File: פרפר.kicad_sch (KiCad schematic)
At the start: 33 parts, among them J1 Conn_01x03_MountingPin, J2 Conn_01x22_Shielded

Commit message: parpar v2 RC2
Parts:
- added D49: TI TSD05C, PCM_Diode_SMD_AKL:D_SOD-323_TVS, symbol PCM_Diode_TVS_AKL:D_TVS_Bidirectional_Generic
- added J5: Conn_01x04_MountingPin, Connector_JST:JST_SH_SM04B-SRSS-TB_1x04-1MP_P1.00mm_Horizontal, symbol Connector_Generic_MountingPin:Conn_01x04_MountingPin
- added JP2: SolderJumper_3_Bridged12, Jumper:SolderJumper-3_P1.3mm_Bridged12_RoundedPad1.0x1.5mm, symbol Jumper:SolderJumper_3_Bridged12
- J1: footprint Connector_JST:JST_PH_S3B-PH-SM4-TB_1x03-1MP_P2.00mm_Horizontal -> Connector_JST:JST_SH_BM03B-SRSS-TB_1x03-1MP_P1.00mm_Vertical
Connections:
- net GND: now also D49.2 (A), J5.1 (Pin_1), J5.MP (MountPin)
- net PRI_LO: now also J5.2 (Pin_2)
- net ec1a: no longer D47.6 (L4)
- net ec1b: no longer D47.4 (L3)
- net ec2a: no longer D47.3 (L2)
- net ec2b: no longer D47.1 (L1)
- net gpio3: now also JP2.1 (A)
- net gpio4: now also J5.4 (Pin_4)
- net c0 renamed col_a
- net c1 renamed col_b
- net c2 renamed col_c
- net c3 renamed col_d
- net c4 renamed col_e
- net c5 renamed col_f
- net row_a renamed row_0
- net row_b renamed row_1
- net row_c renamed row_2
- net row_d renamed row_3
- net row_e renamed row_4
- net row_f renamed row_5
- net row_g renamed row_6
- net row_h renamed row_7
- new net: J5.3 (Pin_3), JP2.2 (C)
- new net emtx_b0: D47.6 (L4)
- new net emtx_b1: D47.4 (L3)
- new net emtx_c0: D47.3 (L2)
- new net emtx_c1: D47.1 (L1)
- new net led_data: D49.1 (K)
- new net led_out: JP2.3 (B)
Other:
- note added: "add-on port"
- note added: "led input"
- note removed: "led power input"
- moved on the sheet: D48

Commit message: parpar v2 RC3
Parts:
- removed JP2: SolderJumper_3_Bridged12, Jumper:SolderJumper-3_P1.3mm_Bridged12_RoundedPad1.0x1.5mm, symbol Jumper:SolderJumper_3_Bridged12
- added J6: Conn_01x02_MountingPin, Connector_JST:JST_SUR_SM02B-SURS-TF_1x02-1MP_P0.80mm_Horizontal, symbol Connector_Generic_MountingPin:Conn_01x02_MountingPin
- added JP2, JP4, JP5: SolderJumper_3_Open, Jumper:SolderJumper-3_P2.0mm_Open_TrianglePad1.0x1.5mm, symbol Jumper:SolderJumper_3_Open
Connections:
- net emtx_b0 is gone; now on net ec1a: D47.6 (L4)
- net emtx_b1 is gone; now on net ec1b: D47.4 (L3)
- net emtx_c0 is gone; now on net ec2a: D47.3 (L2)
- net emtx_c1 is gone; now on net ec2b: D47.1 (L1)
- net GND: now also J6.MP (MountPin), JP5.3 (B); no longer J5.1 (Pin_1)
- net PRI_LO: now also JP4.3 (B); no longer J5.2 (Pin_2)
- net gpio3: now also JP2.1 (A)
- net led_out: now also JP2.3 (B)
- net at J5.3 (Pin_3): now also JP2.2 (C)
- new net: J5.2 (Pin_2), JP4.2 (C)
- new net: J5.1 (Pin_1), JP5.2 (C)
- new net Earth_Clean: J6.2 (Pin_2), JP5.1 (A)
- new net VCC: J6.1 (Pin_1), JP4.1 (A)
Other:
- note added: "mcu vdd in"
- moved on the sheet: J5

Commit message: parpar v2 RC4
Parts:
- removed H1: MountingHole, MountingHole:MountingHole_2.2mm_M2_DIN965, symbol Mechanical:MountingHole
- removed JP5: SolderJumper_3_Open, Jumper:SolderJumper-3_P2.0mm_Open_TrianglePad1.0x1.5mm, symbol Jumper:SolderJumper_3_Open
- added FB3: Ferrite_Bead, PCM_Ferrite_SMD_AKL:Ferrite_0805_2012Metric, symbol PCM_Device_AKL:Ferrite_Bead
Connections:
- net PRI_LO is gone; now on net +5V: D48.1 (K), JP4.3 (B)
- net Earth_Clean: now also FB3.1
- net GND: now also J5.1 (Pin_1), FB3.2
- net led_data renamed led_data_in
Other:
- note removed: "alignment mounting hole"
- moved on the sheet: D1, D2, D45, D46, D47, D48, D49, FB1, FB2, H10, H11, H12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

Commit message: parpar v2 RC6
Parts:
- added J7: JST_SH_BM03B-SRSS-TB, Connector_JST:JST_SH_BM03B-SRSS-TB_1x03-1MP_P1.00mm_Vertical, symbol Connector_Generic_MountingPin:Conn_01x03_MountingPin
- J1: value Conn_01x03_MountingPin -> JST_SH_BM03B-SRSS-TB
- J2: value Conn_01x22_Shielded -> Hirose_FH12-22S-0.5SH
- J5: value Conn_01x04_MountingPin -> JST_SH_SM04B-SRSS-TB
- J6: value Conn_01x02_MountingPin -> JST_SUR_SM02B-SURS-TF
- JP2: value SolderJumper_3_Open -> data select; footprint Jumper:SolderJumper-3_P2.0mm_Open_TrianglePad1.0x1.5mm -> Jumper:SolderJumper-3_P1.3mm_Bridged12_RoundedPad1.0x1.5mm; symbol Jumper:SolderJumper_3_Open -> Jumper:SolderJumper_3_Bridged12
- JP4: value SolderJumper_3_Open -> power select; footprint Jumper:SolderJumper-3_P2.0mm_Open_TrianglePad1.0x1.5mm -> Jumper:SolderJumper-3_P1.3mm_Bridged12_RoundedPad1.0x1.5mm; symbol Jumper:SolderJumper_3_Open -> Jumper:SolderJumper_3_Bridged12
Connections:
- net +5V: now also J7.2 (Pin_2)
- net GND: now also J7.3 (Pin_3), J7.MP (MountPin)
- net led_out: now also J7.1 (Pin_1)
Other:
- note added: "rgb in"
- note added: "rgb out"
- note removed: "led input"

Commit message: coquette parpar mk2 final?
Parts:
- added RN1, RN2: R_4x0603_Concave, PCM_Resistor_SMD_AKL:R_Array_Concave_4x0603, symbol PCM_Resistor_AKL:R_4x0603_Concave
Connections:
- net row_0: now also RN1.5 (R4.2); no longer D1.6 (L4), J2.2 (Pin_2)
- net row_1: now also RN1.6 (R3.2); no longer D1.3 (L2), J2.3 (Pin_3)
- net row_2: now also RN1.7 (R2.2); no longer D1.1 (L1), J2.4 (Pin_4)
- net row_3: now also RN1.8 (R1.2); no longer D1.4 (L3), J2.5 (Pin_5)
- net row_4: now also RN2.5 (R4.2); no longer D2.6 (L4), J2.18 (Pin_18)
- net row_5: now also RN2.6 (R3.2); no longer D2.4 (L3), J2.19 (Pin_19)
- net row_6: now also RN2.7 (R2.2); no longer D2.3 (L2), J2.20 (Pin_20)
- net row_7: now also RN2.8 (R1.2); no longer D2.1 (L1), J2.21 (Pin_21)
- new net row_0_in: D1.6 (L4), J2.2 (Pin_2), RN1.4 (R4.1)
- new net row_1_in: D1.3 (L2), J2.3 (Pin_3), RN1.3 (R3.1)
- new net row_2_in: D1.1 (L1), J2.4 (Pin_4), RN1.2 (R2.1)
- new net row_3_in: D1.4 (L3), J2.5 (Pin_5), RN1.1 (R1.1)
- new net row_4_in: D2.6 (L4), J2.18 (Pin_18), RN2.4 (R4.1)
- new net row_5_in: D2.4 (L3), J2.19 (Pin_19), RN2.3 (R3.1)
- new net row_6_in: D2.3 (L2), J2.20 (Pin_20), RN2.2 (R2.1)
- new net row_7_in: D2.1 (L1), J2.21 (Pin_21), RN2.1 (R1.1)

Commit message: coquette parpar mk2 final? try2
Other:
- note added: "row series resistors"
- moved on the sheet: RN1, RN2
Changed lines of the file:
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@@
 	)
 	(rectangle
+		(start 215.9 98.425)
+		(end 251.46 160.02)
+		(stroke
+			(width 0)
+			(type default)
+		)
+		(fill
+			(type none)
+		)
+	)
+	(rectangle
 		(start 26.67 97.79)
 		(end 71.12 128.27)
@@
 		)
 	)
+	(text "row series resistors"
+		(exclude_from_sim no)
+		(at 225.298 97.79 0)
+		(effects
+			(font
+				(size 1.27 1.27)
+			)
+		)
+	)
 	(text "rgb in"
 		(exclude_from_sim no)
@@
 	(global_label "row_4"
 		(shape input)
-		(at 237.49 140.97 90)
+		(at 228.6 137.16 90)
 		(fields_autoplaced yes)
 		(effects
@@
 		)
 		(property "Intersheetrefs" "${INTERSHEET_REFS}"
-			(at 237.49 133.6103 90)
+			(at 228.6 129.8003 90)
 			(effects
 				(font
@@
 	(global_label "row_5"
 		(shape input)
-		(at 234.95 140.97 90)
+		(at 226.06 137.16 90)
 		(fields_autoplaced yes)
 		(effects
@@
 		)
 		(property "Intersheetrefs" "${INTERSHEET_REFS}"
-			(at 234.95 133.6103 90)
+			(at 226.06 129.8003 90)
 			(effects
 				(font
@@
 	(global_label "row_6"
 		(shape input)
-		(at 232.41 140.97 90)
+		(at 223.52 137.16 90)
 		(fields_autoplaced yes)
 		(effects
@@
 		)
 		(property "Intersheetrefs" "${INTERSHEET_REFS}"
-			(at 232.41 133.6103 90)
+			(at 223.52 129.8003 90)
 			(effects
 				(font
@@
 	(global_label "row_5_in"
 		(shape input)
-		(at 234.95 151.13 270)
+		(at 226.06 147.32 270)
 		(fields_autoplaced yes)
 		(effects
@@
 		)
 		(property "Intersheetrefs" "${INTERSHEET_REFS}"
-			(at 234.95 161.2479 90)
+			(at 226.06 157.4379 90)
 			(effects
 				(font
@@
 	(global_label "row_1_in"
 		(shape input)
-		(at 234.95 121.92 270)
+		(at 226.06 118.11 270)
 		(fields_autoplaced yes)
 		(effects
@@
 		)
 		(property "Intersheetrefs" "${INTERSHEET_REFS}"
-			(at 234.95 132.0379 90)
+			(at 226.06 128.2279 90)
 			(effects
 				(font
@@
 	(global_label "row_0"
 		(shape input)
-		(at 237.49 111.76 90)
+		(at 228.6 107.95 90)
 		(fields_autoplaced yes)
 		(effects
@@
 		)
 		(property "Intersheetrefs" "${INTERSHEET_REFS}"
-			(at 237.49 104.4003 90)
+			(at 228.6 100.5903 90)
 			(effects
 				(font
@@
 	(global_label "row_3_in"
 		(shape input)
-		(at 229.87 121.92 270)
+		(at 220.98 118.11 270)
 		(fields_autoplaced yes)
 		(effects
@@
 		)
 		(property "Intersheetrefs" "${INTERSHEET_REFS}"
-			(at 229.87 132.0379 90)
+			(at 220.98 128.2279 90)
 			(effects
 				(font
@@
 	(global_label "row_1"
 		(shape input)
-		(at 234.95 111.76 90)
+		(at 226.06 107.95 90)
 		(fields_autoplaced yes)
 		(effects
@@
 		)
 		(property "Intersheetrefs" "${INTERSHEET_REFS}"
-			(at 234.95 104.4003 90)
+			(at 226.06 100.5903 90)
 			(effects
 				(font
@@
 	(global_label "row_2_in"
 		(shape input)
-		(at 232.41 121.92 270)
+		(at 223.52 118.11 270)
 		(fields_autoplaced yes)
 		(effects
@@
 		)
 		(property "Intersheetrefs" "${INTERSHEET_REFS}"
-			(at 232.41 132.0379 90)
+			(at 223.52 128.2279 90)
 			(effects
 				(font
@@
 	(global_label "row_0_in"
 		(shape input)
-		(at 237.49 121.92 270)
+		(at 228.6 118.11 270)
 		(fields_autoplaced yes)
 		(effects
@@
 		)
 		(property "Intersheetrefs" "${INTERSHEET_REFS}"
-			(at 237.49 132.0379 90)
+			(at 228.6 128.2279 90)
 			(effects
 				(font
@@
 	(global_label "row_4_in"
 		(shape input)
-		(at 237.49 151.13 270)
+		(at 228.6 147.32 270)
 		(fields_autoplaced yes)
 		(effects
@@
 		)
 		(property "Intersheetrefs" "${INTERSHEET_REFS}"
-			(at 237.49 161.2479 90)
+			(at 228.6 157.4379 90)
 			(effects
 				(font
@@
 	(global_label "row_3"
 		(shape input)
-		(at 229.87 111.76 90)
+		(at 220.98 107.95 90)
 		(fields_autoplaced yes)
 		(effects
@@
 		)
 		(property "Intersheetrefs" "${INTERSHEET_REFS}"
-			(at 229.87 104.4003 90)
+			(at 220.98 100.5903 90)
 			(effects
 				(font
@@
 	(global_label "row_7_in"
 		(shape input)
-		(at 229.87 151.13 270)
+		(at 220.98 147.32 270)
 		(fields_autoplaced yes)
 		(effects
@@
 		)
 		(property "Intersheetrefs" "${INTERSHEET_REFS}"
-			(at 229.87 161.2479 90)
+			(at 220.98 157.4379 90)
 			(effects
 				(font
@@
 	(global_label "row_2"
 		(shape input)
-		(at 232.41 111.76 90)
+		(at 223.52 107.95 90)
 		(fields_autoplaced yes)
 		(effects
@@
 		)
 		(property "Intersheetrefs" "${INTERSHEET_REFS}"
-			(at 232.41 104.4003 90)
+			(at 223.52 100.5903 90)
 			(effects
 				(font
@@
 	(global_label "row_7"
 		(shape input)
-		(at 229.87 140.97 90)
+		(at 220.98 137.16 90)
 		(fields_autoplaced yes)
 		(effects
@@
 		)
 		(property "Intersheetrefs" "${INTERSHEET_REFS}"
-			(at 229.87 133.6103 90)
+			(at 220.98 129.8003 90)
 			(effects
 				(font
@@
 	(global_label "row_6_in"
 		(shape input)
-		(at 232.41 151.13 270)
+		(at 223.52 147.32 270)
 		(fields_autoplaced yes)
 		(effects
@@
 		)
 		(property "Intersheetrefs" "${INTERSHEET_REFS}"
-			(at 232.41 161.2479 90)
+			(at 223.52 157.4379 90)
 			(effects
 				(font
@@
 	(symbol
 		(lib_id "PCM_Resistor_AKL:R_4x0603_Concave")
-		(at 234.95 116.84 0)
+		(at 226.06 113.03 0)
 		(unit 1)
 		(exclude_from_sim no)
@@
 		(fields_autoplaced yes)
 		(property "Reference" "RN1"
-			(at 240.03 115.5699 0)
+			(at 231.14 111.7599 0)
 			(effects
 				(font
@@
 		)
 		(property "Value" "R_4x0603_Concave"
-			(at 240.03 118.1099 0)
+			(at 231.14 114.2999 0)
 			(effects
 				(font
@@
 		)
 		(property "Footprint" "PCM_Resistor_SMD_AKL:R_Array_Concave_4x0603"
-			(at 234.95 129.54 0)
+			(at 226.06 125.73 0)
 			(effects
 				(font
@@
 		)
 		(property "Datasheet" "~"
-			(at 234.95 116.84 0)
+			(at 226.06 113.03 0)
 			(effects
 				(font
@@
 		)
 		(property "Description" "4x0603 SMD Resistor Network, Isolated, European Symbol, Alternate KiCad Library"
-			(at 234.95 116.84 0)
+			(at 226.06 113.03 0)
 			(effects
 				(font
@@
 	(symbol
 		(lib_id "PCM_Resistor_AKL:R_4x0603_Concave")
-		(at 234.95 146.05 0)
+		(at 226.06 142.24 0)
 		(unit 1)
 		(exclude_from_sim no)
@@
 		(fields_autoplaced yes)
 		(property "Reference" "RN2"
-			(at 240.03 144.7799 0)
+			(at 231.14 140.9699 0)
 			(effects
 				(font
@@
 		)
 		(property "Value" "R_4x0603_Concave"
-			(at 240.03 147.3199 0)
+			(at 231.14 143.5099 0)
 			(effects
 				(font
@@
 		)
 		(property "Footprint" "PCM_Resistor_SMD_AKL:R_Array_Concave_4x0603"
-			(at 234.95 158.75 0)
+			(at 226.06 154.94 0)
 			(effects
 				(font
@@
 		)
 		(property "Datasheet" "~"
-			(at 234.95 146.05 0)
+			(at 226.06 142.24 0)
 			(effects
 				(font
@@
 		)
 		(property "Description" "4x0603 SMD Resistor Network, Isolated, European Symbol, Alternate KiCad Library"
-			(at 234.95 146.05 0)
+			(at 226.06 142.24 0)
 			(effects
 				(font

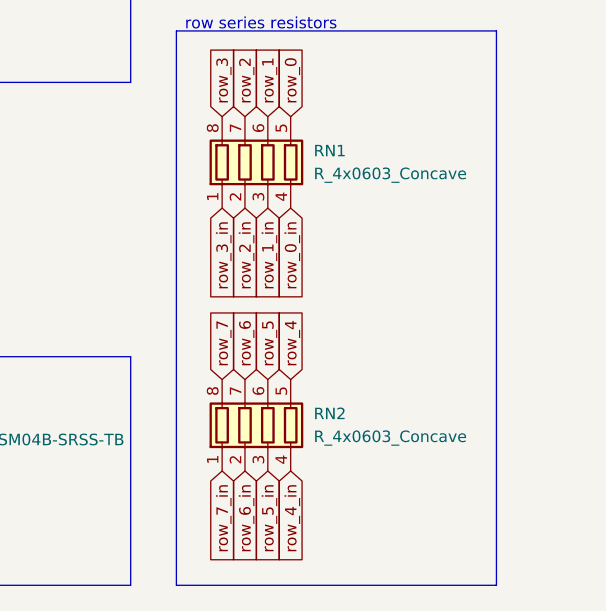
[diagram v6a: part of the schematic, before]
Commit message: change resistor network value to one readily available
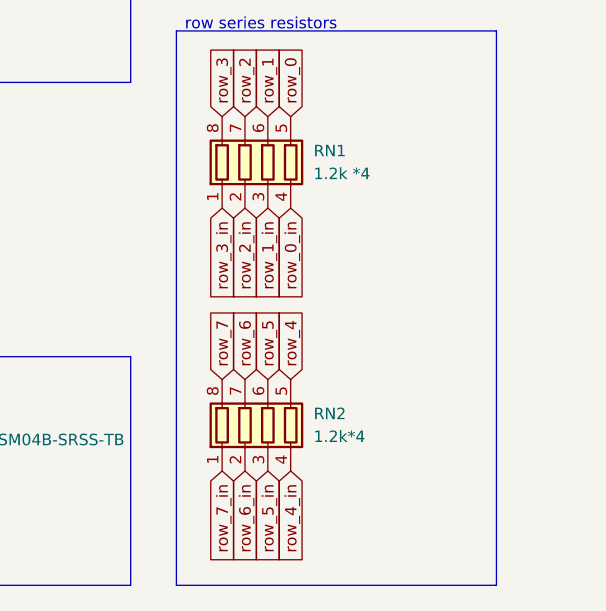
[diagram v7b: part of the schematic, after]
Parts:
- RN1: value R_4x0603_Concave -> 1.2k *4
- RN2: value R_4x0603_Concave -> 1.2k*4
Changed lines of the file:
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@@
 			)
 		)
-		(property "Value" "R_4x0603_Concave"
+		(property "Value" "1.2k *4"
 			(at 231.14 114.2999 0)
 			(effects
@@
 			)
 		)
-		(property "Value" "R_4x0603_Concave"
+		(property "Value" "1.2k*4"
 			(at 231.14 143.5099 0)
 			(effects

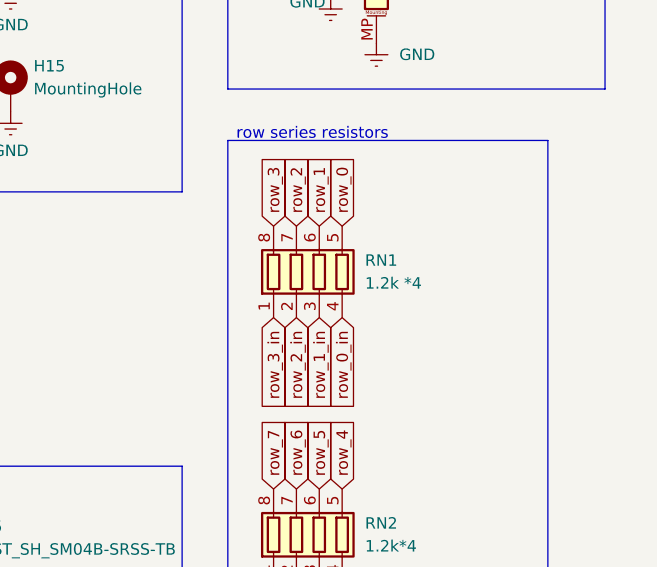
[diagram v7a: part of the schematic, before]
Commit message: another resistor value to a real-world existing part
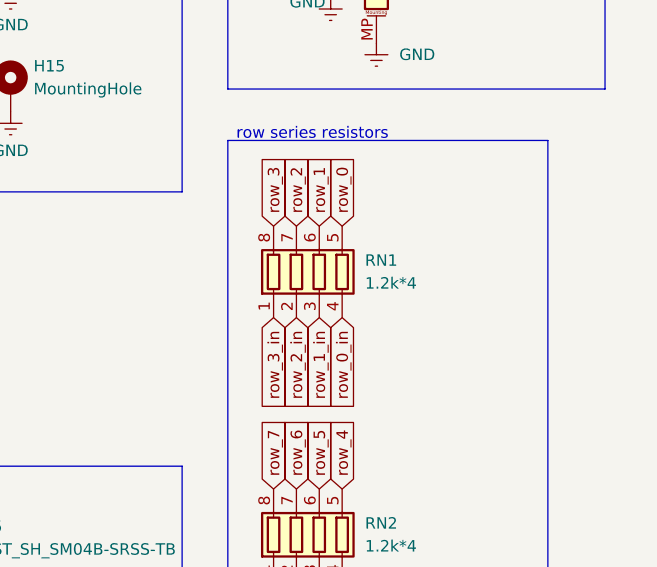
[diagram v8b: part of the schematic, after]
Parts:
- RN1: value 1.2k *4 -> 1.2k*4
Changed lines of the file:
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@@
 			)
 		)
-		(property "Value" "1.2k *4"
+		(property "Value" "1.2k*4"
 			(at 231.14 114.2999 0)
 			(effects
